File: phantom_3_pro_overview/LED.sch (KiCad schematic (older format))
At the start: 0 parts

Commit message: Overview: LED board update.
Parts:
- added D1: LED_RGB_5050, symbol LED_RGB
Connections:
- new net: D1.4 (BA), D1.5 (GA), D1.6 (RA)
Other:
- note added: "LED driver here"
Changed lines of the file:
@@
 EELAYER 25 0
 EELAYER END
-$Descr A4 11693 8268
+$Descr User 5354 4724
 encoding utf-8
-Sheet 19 23
+Sheet 16 23
 Title ""
 Date ""
@@
 $EndDescr
 Wire Bus Line
-	3750 2250 4250 2250
-Text HLabel 4250 2250 2    60   Input ~ 0
+	1950 1000 1950 1850
+Text HLabel 1950 1000 1    60   Input ~ 0
 CTRL
+$Comp
+L LED_RGB D1
+U 1 1 596DFE26
+P 1150 1550
+F 0 "D1" H 1150 1920 50  0000 C CNN
+F 1 "LED_RGB_5050" H 1150 1200 50  0000 C CNN
+F 2 "" H 1150 1500 50  0001 C CNN
+F 3 "" H 1150 1500 50  0001 C CNN
+	1    1150 1550
+	0    -1   -1   0
+$EndComp
+Wire Wire Line
+	950  1350 950  1300
+Wire Wire Line
+	950  1300 1850 1300
+Wire Wire Line
+	1350 1300 1350 1350
+Wire Wire Line
+	1150 1350 1150 1300
+Connection ~ 1150 1300
+Entry Wire Line
+	1850 1300 1950 1200
+Connection ~ 1350 1300
+Entry Wire Line
+	1850 1950 1950 1850
+Entry Wire Line
+	1850 1800 1950 1700
+Text Notes 850  1950 0    60   ~ 0
+LED driver here
 $EndSCHEMATC

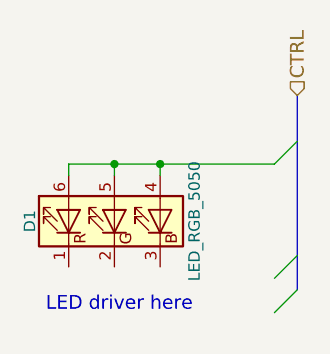
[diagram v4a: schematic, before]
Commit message: Overview: Updated LED board to match reality.
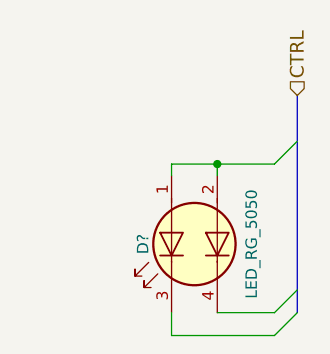
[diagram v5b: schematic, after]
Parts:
- removed D1: LED_RGB_5050, symbol LED_RGB
- added D?: LED_RG_5050, symbol LED_Dual_AACC
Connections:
- new net: D?.1 (A1), D?.2 (A2)
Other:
- note removed: "LED driver here"
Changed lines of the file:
@@
 $EndDescr
 Wire Bus Line
-	1950 1000 1950 1850
+	1950 1000 1950 1950
 Text HLabel 1950 1000 1    60   Input ~ 0
 CTRL
+Wire Wire Line
+	1400 1350 1400 1300
+Wire Wire Line
+	1400 1300 1850 1300
+Wire Wire Line
+	1600 1350 1600 1300
+Connection ~ 1600 1300
+Entry Wire Line
+	1850 1300 1950 1200
+Entry Wire Line
+	1850 2050 1950 1950
+Entry Wire Line
+	1850 1950 1950 1850
 $Comp
-L LED_RGB D1
-U 1 1 596DFE26
-P 1150 1550
-AR Path="/596E1317/596DFE26" Ref="D1"  Part="1"
-AR Path="/596E06B8/596DFE26" Ref="D1"  Part="1"
-AR Path="/596E11F0/596DFE26" Ref="D1"  Part="1"
-F 0 "D1" H 1150 1920 50  0000 C CNN
-F 1 "LED_RGB_5050" H 1150 1200 50  0000 C CNN
-F 2 "" H 1150 1500 50  0001 C CNN
-F 3 "" H 1150 1500 50  0001 C CNN
-	1    1150 1550
-	0    -1   -1   0
+L LED_Dual_AACC D?
+U 1 1 5979235D
+P 1500 1650
+F 0 "D?" H 1500 1875 50  0000 C CNN
+F 1 "LED_RG_5050" H 1500 1400 50  0000 C CNN
+F 2 "" H 1530 1650 50  0001 C CNN
+F 3 "" H 1530 1650 50  0001 C CNN
+	1    1500 1650
+	0    -1   1    0
 $EndComp
 Wire Wire Line
-	950  1350 950  1300
+	1600 1950 1850 1950
 Wire Wire Line
-	950  1300 1850 1300
+	1850 2050 1400 2050
 Wire Wire Line
-	1350 1300 1350 1350
-Wire Wire Line
-	1150 1350 1150 1300
-Connection ~ 1150 1300
-Entry Wire Line
-	1850 1300 1950 1200
-Connection ~ 1350 1300
-Entry Wire Line
-	1850 1950 1950 1850
-Entry Wire Line
-	1850 1800 1950 1700
-Text Notes 850  1950 0    60   ~ 0
-LED driver here
+	1400 2050 1400 1950
 $EndSCHEMATC

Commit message: Overview: Upgraded to KiCAD 5.0.1.
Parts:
- D?: symbol LED_Dual_AACC -> Device:LED_Dual_AACC
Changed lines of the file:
@@
-EESchema Schematic File Version 2
-LIBS:power
-LIBS:device
-LIBS:transistors
-LIBS:conn
-LIBS:linear
-LIBS:regul
-LIBS:74xx
-LIBS:cmos4000
-LIBS:adc-dac
-LIBS:memory
-LIBS:xilinx
-LIBS:microcontrollers
-LIBS:dsp
-LIBS:microchip
-LIBS:analog_switches
-LIBS:motorola
-LIBS:texas
-LIBS:intel
-LIBS:audio
-LIBS:interface
-LIBS:digital-audio
-LIBS:philips
-LIBS:display
-LIBS:cypress
-LIBS:siliconi
-LIBS:opto
-LIBS:atmel
-LIBS:contrib
-LIBS:valves
-LIBS:motors
-LIBS:ic_dil_generic
-LIBS:sensors
-LIBS:u-blox
-LIBS:amplifiers
-LIBS:transistors-switches
-LIBS:transistors-power
-LIBS:sensors-v2
-LIBS:regul-v2
+EESchema Schematic File Version 4
 LIBS:phantom_3_pro_overview-cache
-EELAYER 25 0
+EELAYER 26 0
 EELAYER END
 $Descr User 5354 4724
@@
 	1850 1950 1950 1850
 $Comp
-L LED_Dual_AACC D?
+L Device:LED_Dual_AACC D?
 U 1 1 5979235D
 P 1500 1650
